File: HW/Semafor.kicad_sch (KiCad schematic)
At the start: 67 parts, among them J1 USB_C_Receptacle_USB2.0, J2 USB_plug, M1 Motor_DC, Q2 Q_PMOS_GSD, Q3 Q_NMOS_GSD, Q4 Q_NMOS_GSD, SW6 SW_SPDT, U1 ESP32-C3, U2 CN3058E, U3 LT1930, U4 E22-900T22D, U5 AT42QT1070-S

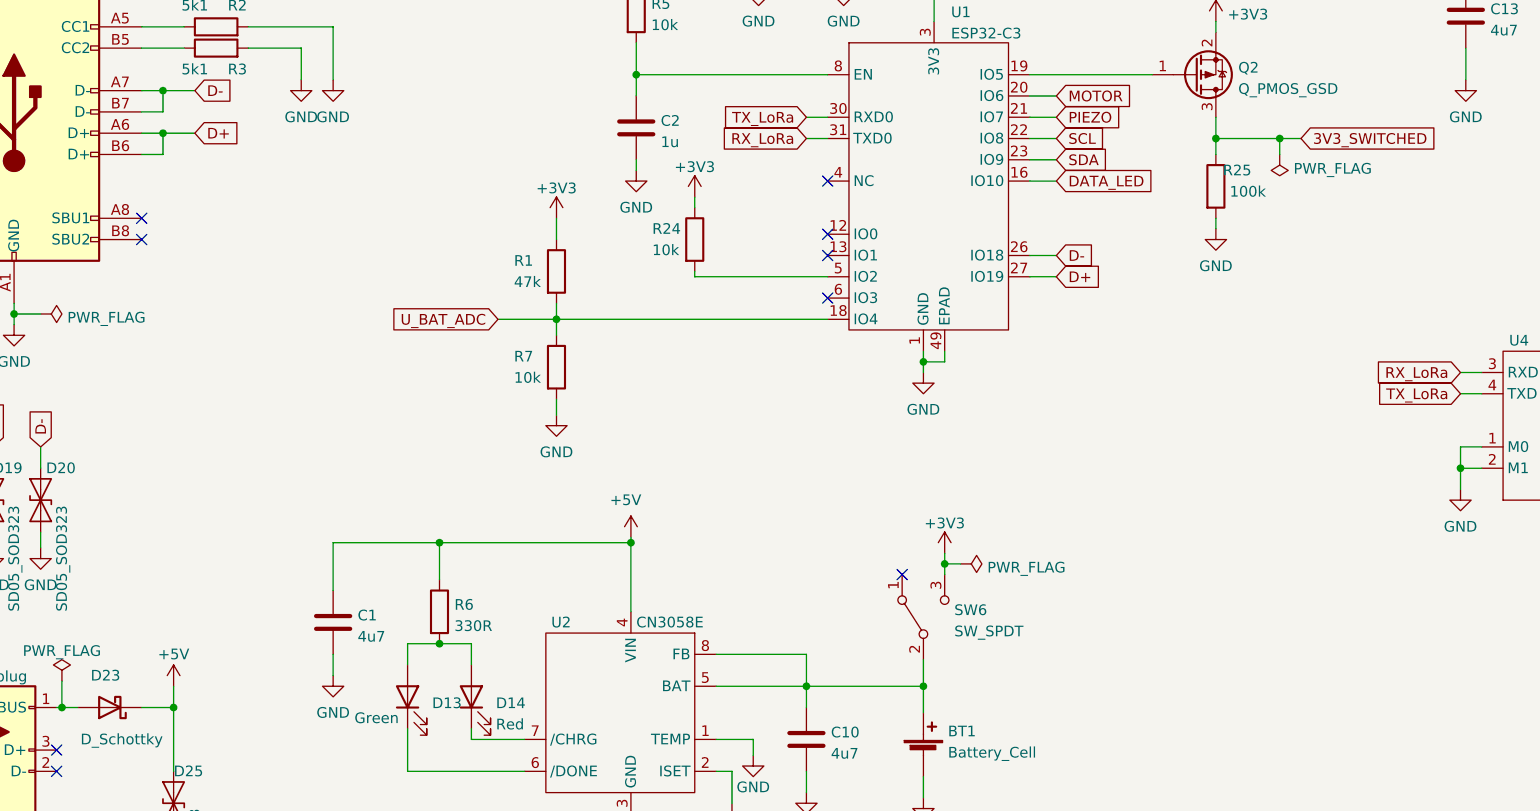
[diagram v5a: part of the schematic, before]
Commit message: add phototransistor and connector for programmable LEDs (on side)
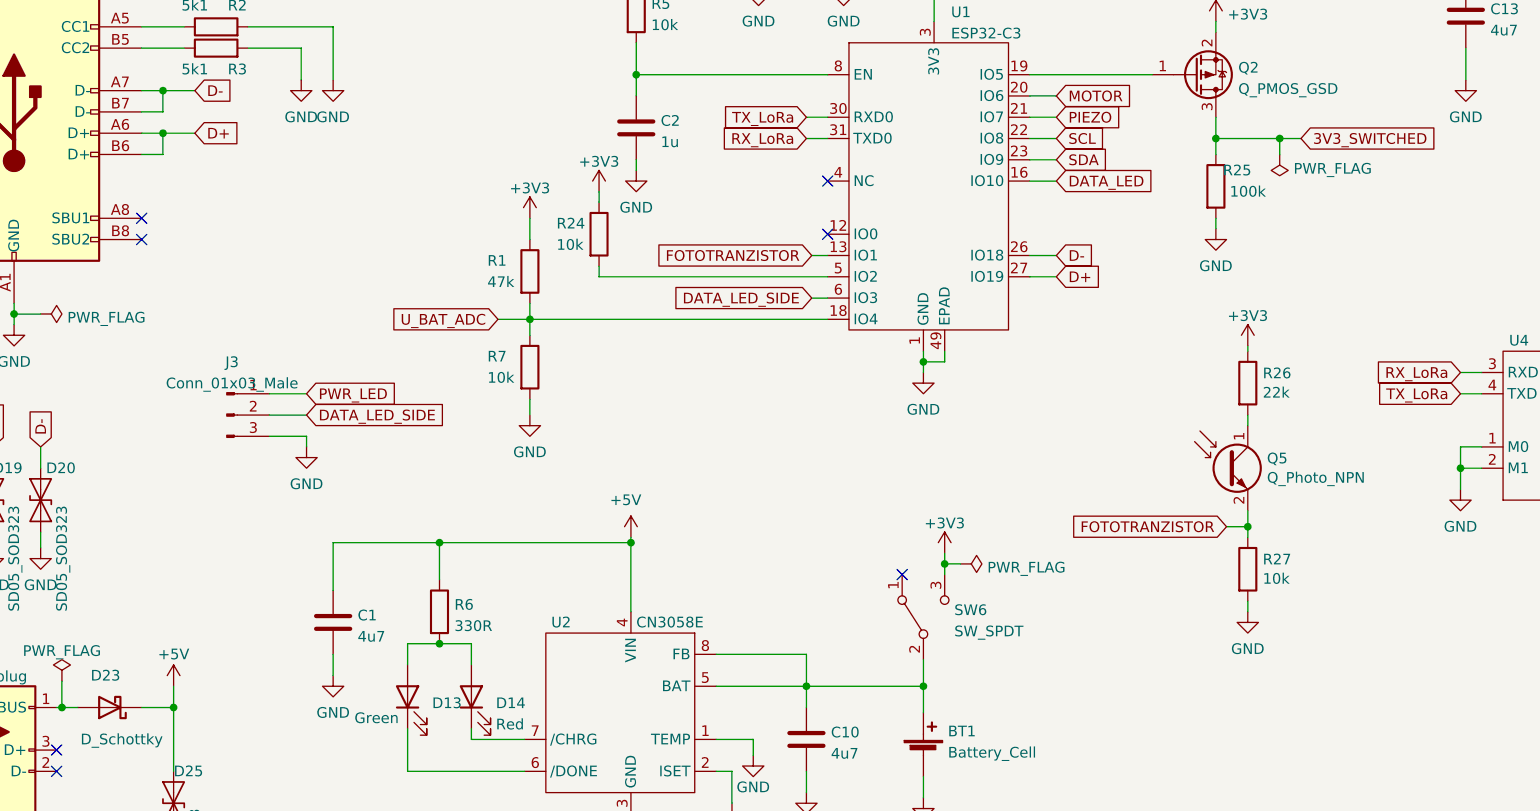
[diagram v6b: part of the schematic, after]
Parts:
- added J3: Conn_01x03_Male, Connector_PinSocket_2.54mm:PinSocket_1x03_P2.54mm_Vertical, symbol Connector:Conn_01x03_Male
- added Q5: Q_Photo_NPN, Library:SMD,3.5x2.8x1.9mm, symbol Device:Q_Photo_NPN
- added R26: 22k, Resistor_SMD:R_0402_1005Metric, symbol Device:R
- added R27: 10k, Resistor_SMD:R_0402_1005Metric, symbol Device:R
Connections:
- net +3V3: now also R26.1
- net GND: now also J3.3 (Pin_3), R27.2
- net PWR_LED: now also J3.1 (Pin_1)
- net FOTOTRANZISTOR: now reaches U1.13 (IO1)
- net FOTOTRANZISTOR: now also Q5.2 (E), R27.1
- net DATA_LED_SIDE: now reaches U1.6 (IO3)
- net DATA_LED_SIDE: now also J3.2 (Pin_2)
- new net: Q5.1 (C), R26.2
- no-connect marks 14 -> 12
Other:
- moved on the sheet: R1, R24, R7

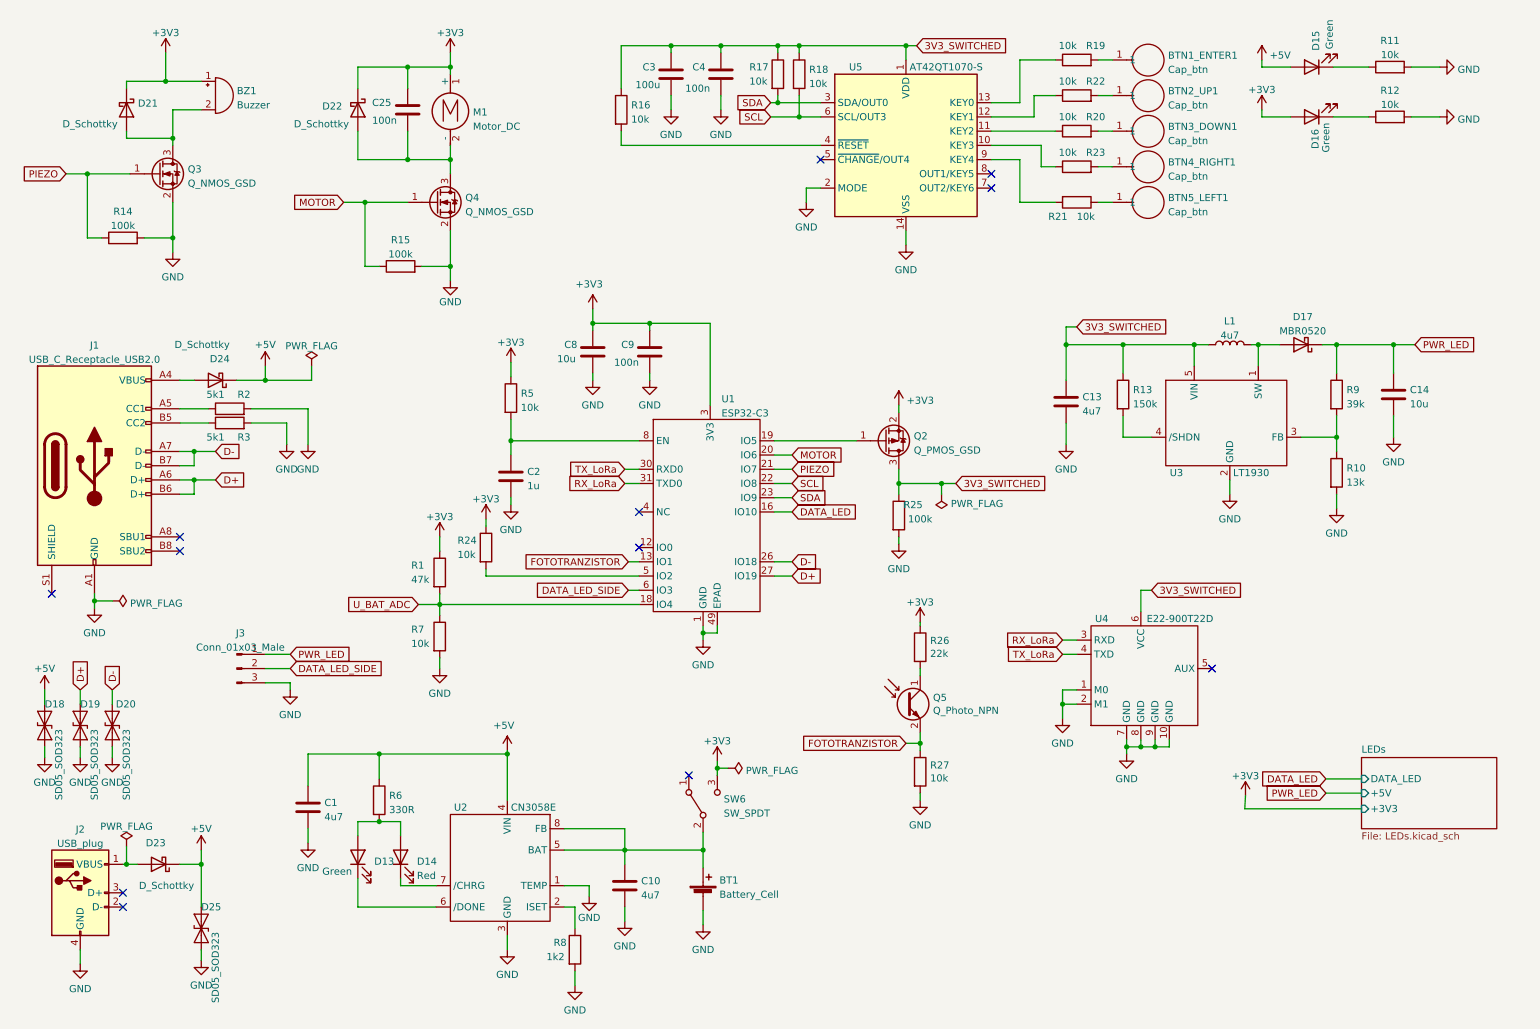
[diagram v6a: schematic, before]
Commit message: start drawing small version of Module, draw stepup as per datasheet
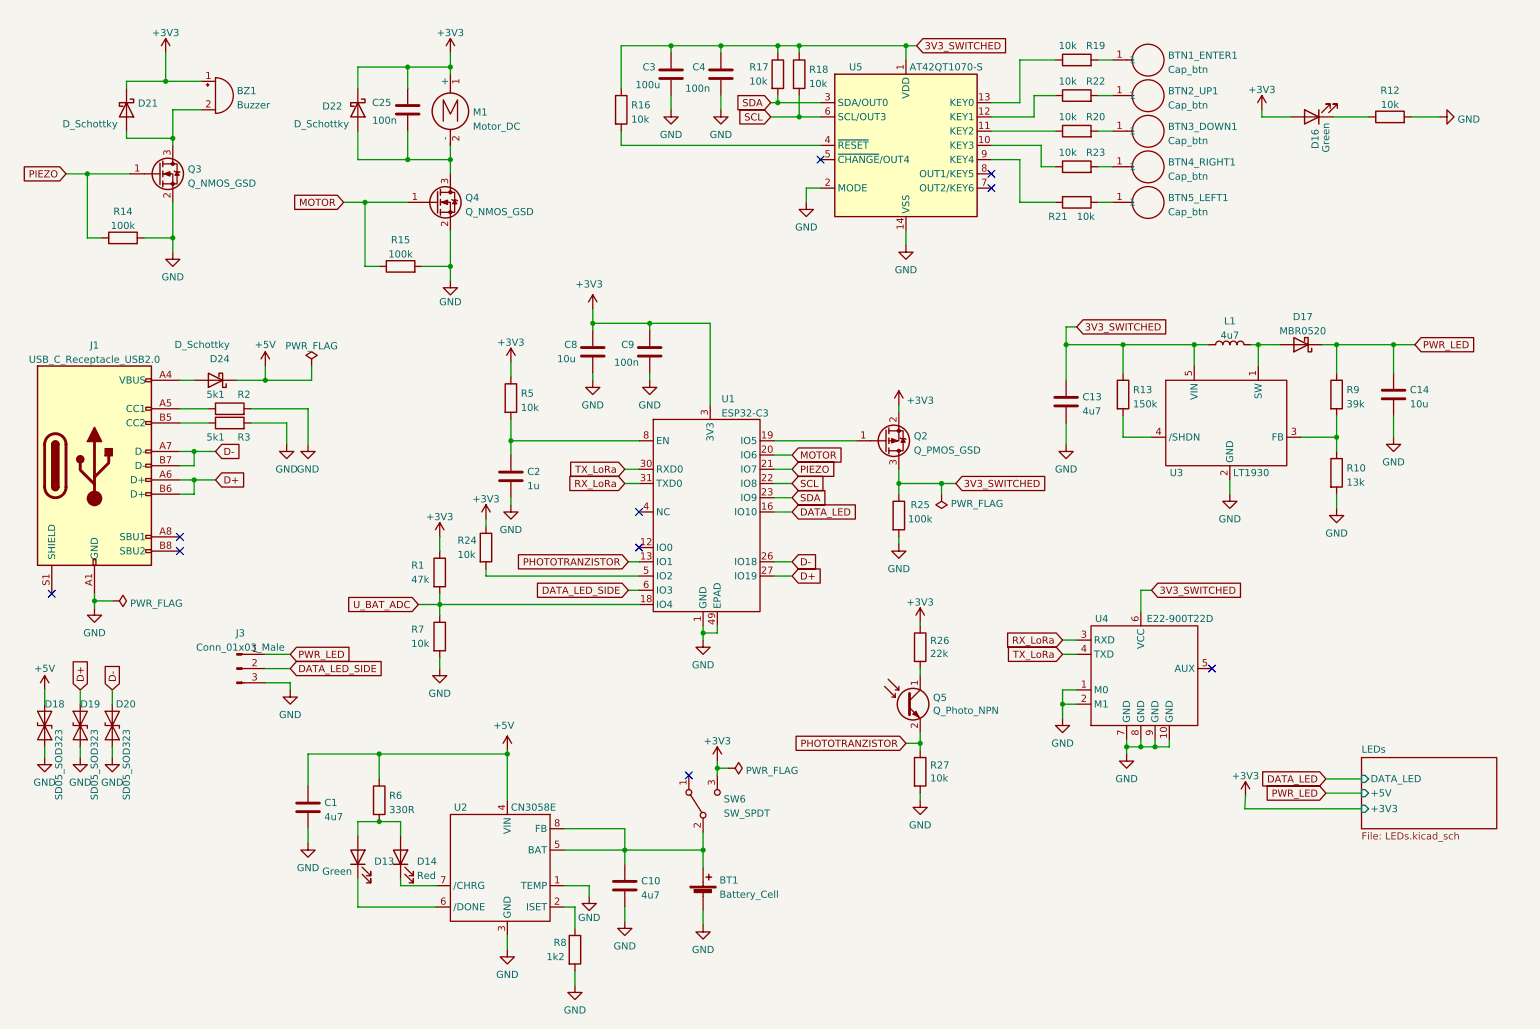
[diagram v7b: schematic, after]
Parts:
- removed D15: Green, LED_SMD:LED_0603_1608Metric, symbol Device:LED
- removed D23: D_Schottky, Diode_SMD:D_SOD-123, symbol Device:D_Schottky
- removed D25: SD05_SOD323, Diode_SMD:D_SOD-323, symbol Diode:SD05_SOD323
- removed J2: USB_plug, Library:USB_plug, symbol Library:USB_plug
- removed R11: 10k, Resistor_SMD:R_0603_1608Metric, symbol Device:R
- BTN1_ENTER1: footprint Library:Cap_btn_5x5 -> Library:Cap_btn_2,5x2,5
- BTN2_UP1, BTN3_DOWN1, BTN4_RIGHT1, BTN5_LEFT1: footprint Library:Cap_btn_2x2 -> Library:Cap_btn_1,6x1,6
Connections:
- net FOTOTRANZISTOR renamed PHOTOTRANZISTOR
- no-connect marks 12 -> 10

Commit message: continue routing
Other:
- moved on the sheet: C13, C14, C2, C8, C9, D16, D17, L1, Q2, Q5, R1, R10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
